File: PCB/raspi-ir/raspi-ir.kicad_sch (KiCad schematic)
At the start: 7 parts, among them J1 Conn_02x16_Odd_Even, J2 Conn_01x02_Pin, Q1 MMBT2222A, U1 TSOP382xx

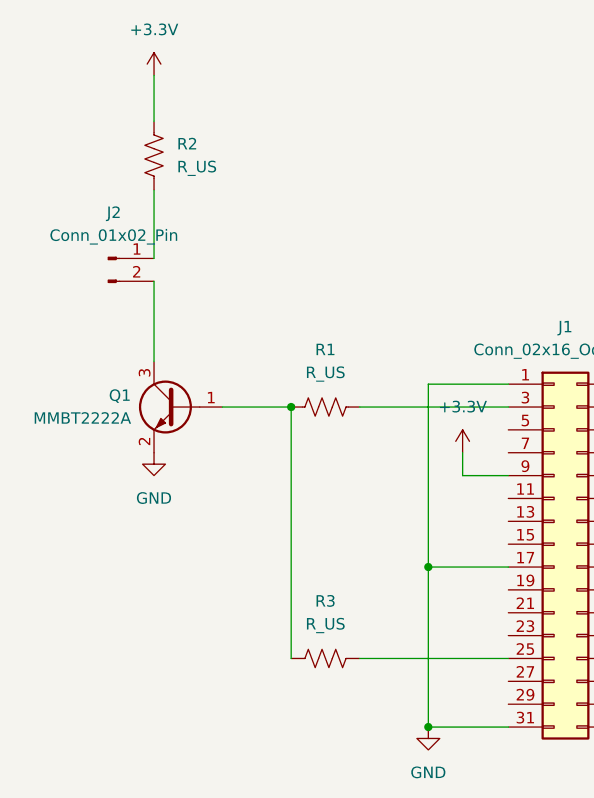
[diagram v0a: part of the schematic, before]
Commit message: New button renderings. Added lirc remotes.
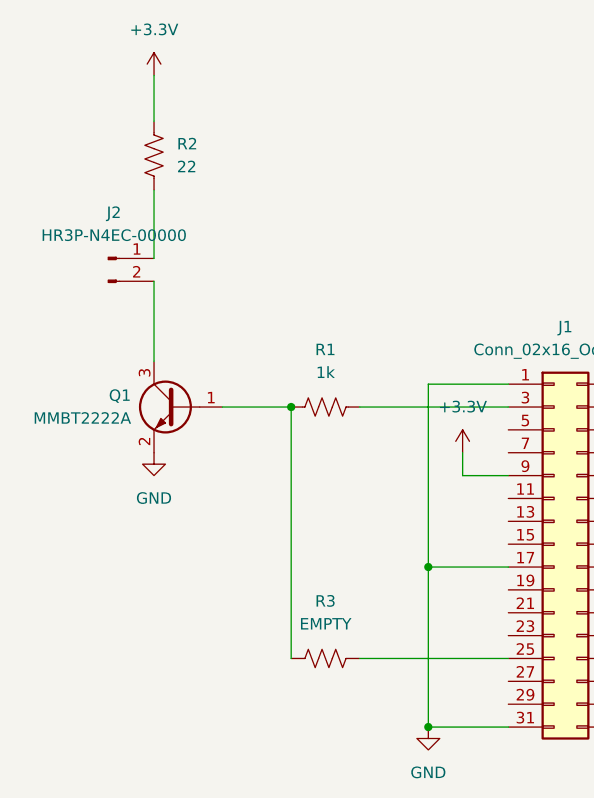
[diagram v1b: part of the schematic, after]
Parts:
- J2: value Conn_01x02_Pin -> HR3P-N4EC-00000; Digikey (none) -> 516-HR3P-N4EC-00000-ND
- R1: value R_US -> 1k
- R2: value R_US -> 22
- R3: value R_US -> EMPTY
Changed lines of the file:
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@@
 			)
 		)
-		(property "Value" "R_US"
+		(property "Value" "EMPTY"
 			(at 120.65 95.25 90)
 			(effects
@@
 			)
 		)
-		(property "Description" "Resistor, US symbol"
+		(property "Description" "Secondary option if PWM output is needed."
 			(at 120.65 99.06 0)
 			(effects
@@
 			)
 		)
-		(property "Value" "R_US"
+		(property "Value" "22"
 			(at 104.14 44.4499 0)
 			(effects
@@
 			)
 		)
-		(property "Value" "R_US"
+		(property "Value" "1k"
 			(at 120.65 67.31 90)
 			(effects
@@
 			)
 		)
-		(property "Value" "Conn_01x02_Pin"
+		(property "Value" "HR3P-N4EC-00000"
 			(at 97.155 52.07 0)
 			(effects
@@
 			)
 		)
-		(property "Description" "Generic connector, single row, 01x02, script generated"
+		(property "Description" "Infrared LED transmitter"
 			(at 96.52 54.61 0)
 			(effects
+				(font
+					(size 1.27 1.27)
+				)
+				(hide yes)
+			)
+		)
+		(property "Digikey" "516-HR3P-N4EC-00000-ND"
+			(at 96.52 54.61 0)
+			(effects

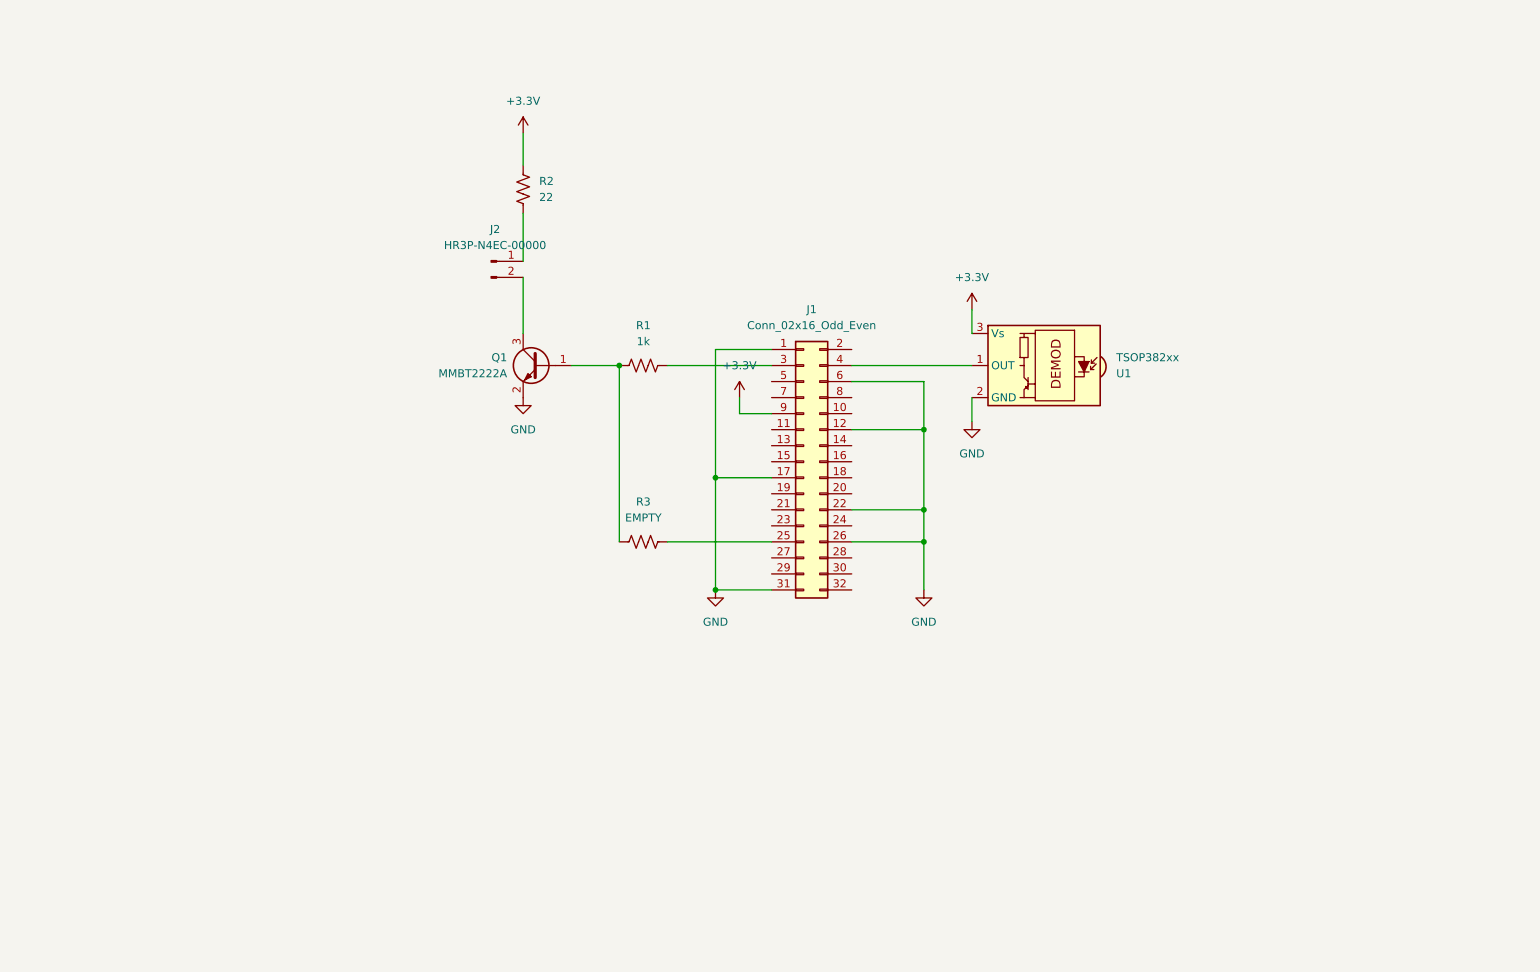
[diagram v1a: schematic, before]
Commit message: Restructured icon files. Updating PCB with more features. Created conference room layout.
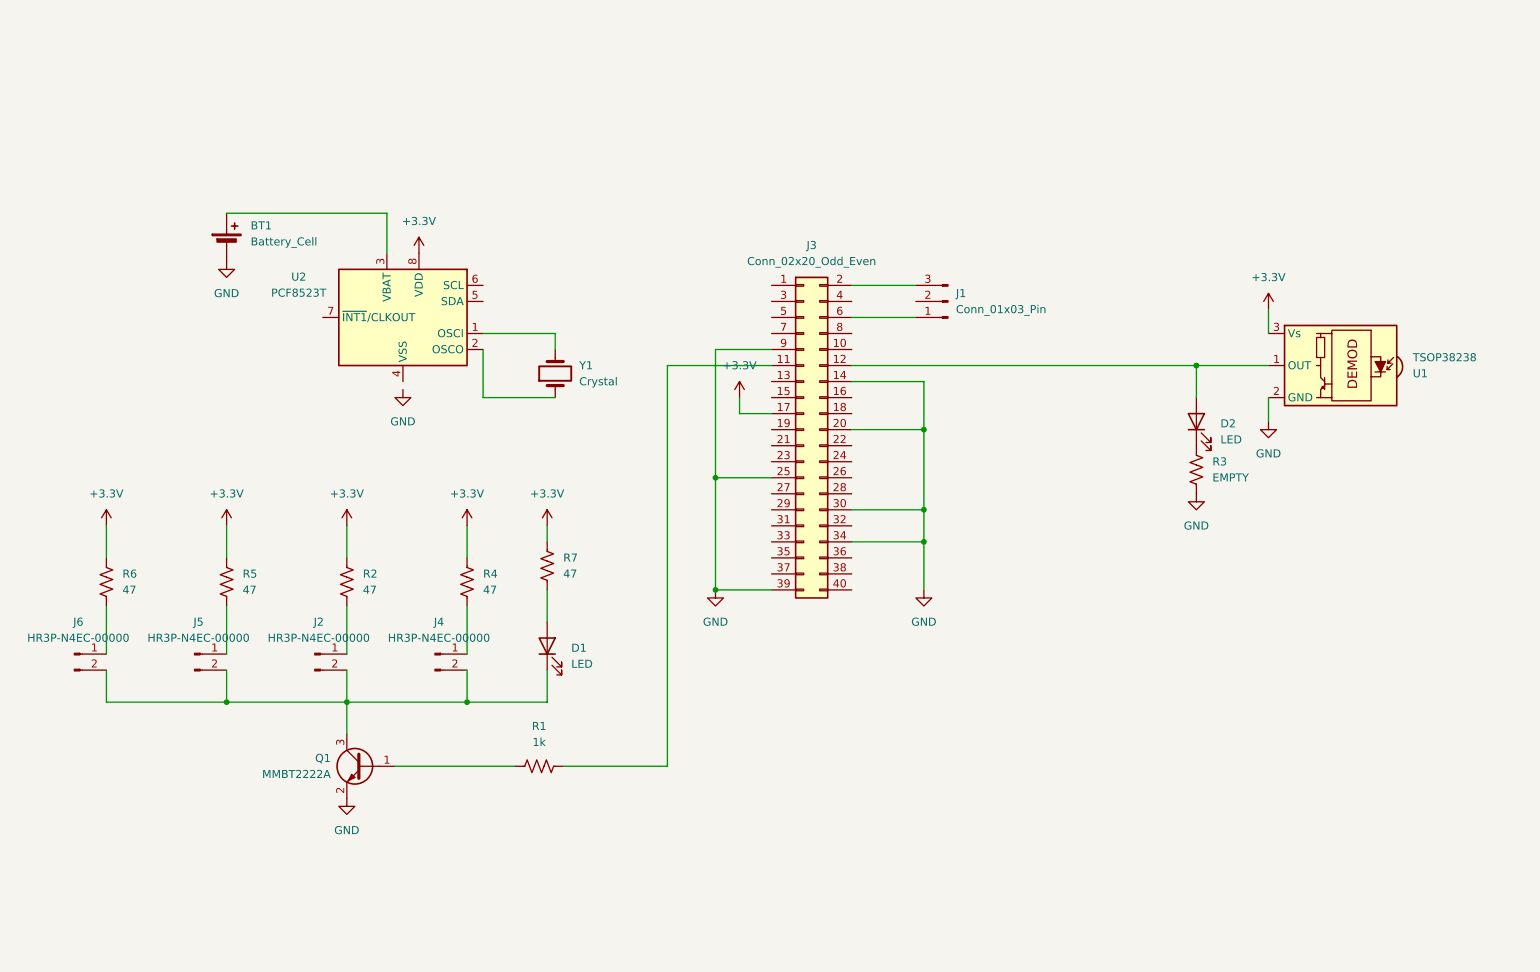
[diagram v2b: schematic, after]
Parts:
- removed J1: Conn_02x16_Odd_Even, Connector_PinHeader_2.54mm:PinHeader_2x16_P2.54mm_Vertical, symbol Connector_Generic:Conn_02x16_Odd_Even
- added BT1: Battery_Cell, Battery:BatteryHolder_Keystone_3000_1x12mm, symbol Device:Battery_Cell
- added D1, D2: LED, Diode_SMD:D_0805_2012Metric, symbol Device:LED
- added J1: Conn_01x03_Pin, Connector_PinSocket_2.54mm:PinSocket_1x03_P2.54mm_Horizontal, symbol Connector:Conn_01x03_Pin
- added J3: Conn_02x20_Odd_Even, Connector_PinHeader_2.54mm:PinHeader_2x20_P2.54mm_Vertical, symbol Connector_Generic:Conn_02x20_Odd_Even
- added J4, J5, J6: HR3P-N4EC-00000, Connector_PinHeader_2.54mm:PinHeader_1x02_P2.54mm_Horizontal, symbol Connector:Conn_01x02_Pin
- added R4, R5, R6, R7: 47, Resistor_SMD:R_0805_2012Metric, symbol Device:R_US
- added U2: PCF8523T, Package_SO:SOIC-8_3.9x4.9mm_P1.27mm, symbol Timer_RTC:PCF8523T
- added Y1: Crystal, Crystal:Crystal_SMD_3215-2Pin_3.2x1.5mm, symbol Device:Crystal
- J2: footprint Connector_PinHeader_2.54mm:PinHeader_1x02_P2.54mm_Vertical -> Connector_PinHeader_2.54mm:PinHeader_1x02_P2.54mm_Horizontal
- Q1: Digikey (none) -> 4878-MMBT2222ATR-ND
- R2: value 22 -> 47; Digikey (none) -> RHM47BTR-ND
- U1: value TSOP382xx -> TSOP38238; Digikey (none) -> 751-1227-ND
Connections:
- net +3.3V: now also J3.17 (Pin_17), R4.1, R5.1, R6.1, R7.1, U2.8 (VDD)
- net GND: now also R3.1, BT1.2 (-), J3.14 (Pin_14), J3.20 (Pin_20), J3.25 (Pin_25), J3.30 (Pin_30), J3.34 (Pin_34), J3.39 (Pin_39), J3.9 (Pin_9)
- net at Q1.1 (B), R1.1: no longer R3.1
- net at R3.2: now also D2.1 (K)
- net at U1.1 (OUT): now also D2.2 (A), J3.12 (Pin_12)
- net at R1.2: now also J3.11 (Pin_11)
- net at J2.2 (Pin_2), Q1.3 (C): now also D1.1 (K), J4.2 (Pin_2), J5.2 (Pin_2), J6.2 (Pin_2)
- new net: J5.1 (Pin_1), R5.2
- new net: BT1.1 (+), U2.3 (VBAT)
- new net: U2.2 (OSCO), Y1.1
- new net: U2.1 (OSCI), Y1.2
- new net: J4.1 (Pin_1), R4.2
- new net: J6.1 (Pin_1), R6.2
- new net: D1.2 (A), R7.2
- new net: J1.1 (Pin_1), J3.6 (Pin_6)
- new net: J1.3 (Pin_3), J3.2 (Pin_2)
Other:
- moved on the sheet: J2, Q1, R1, R2, R3, U1

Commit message: Fix for fan position on case
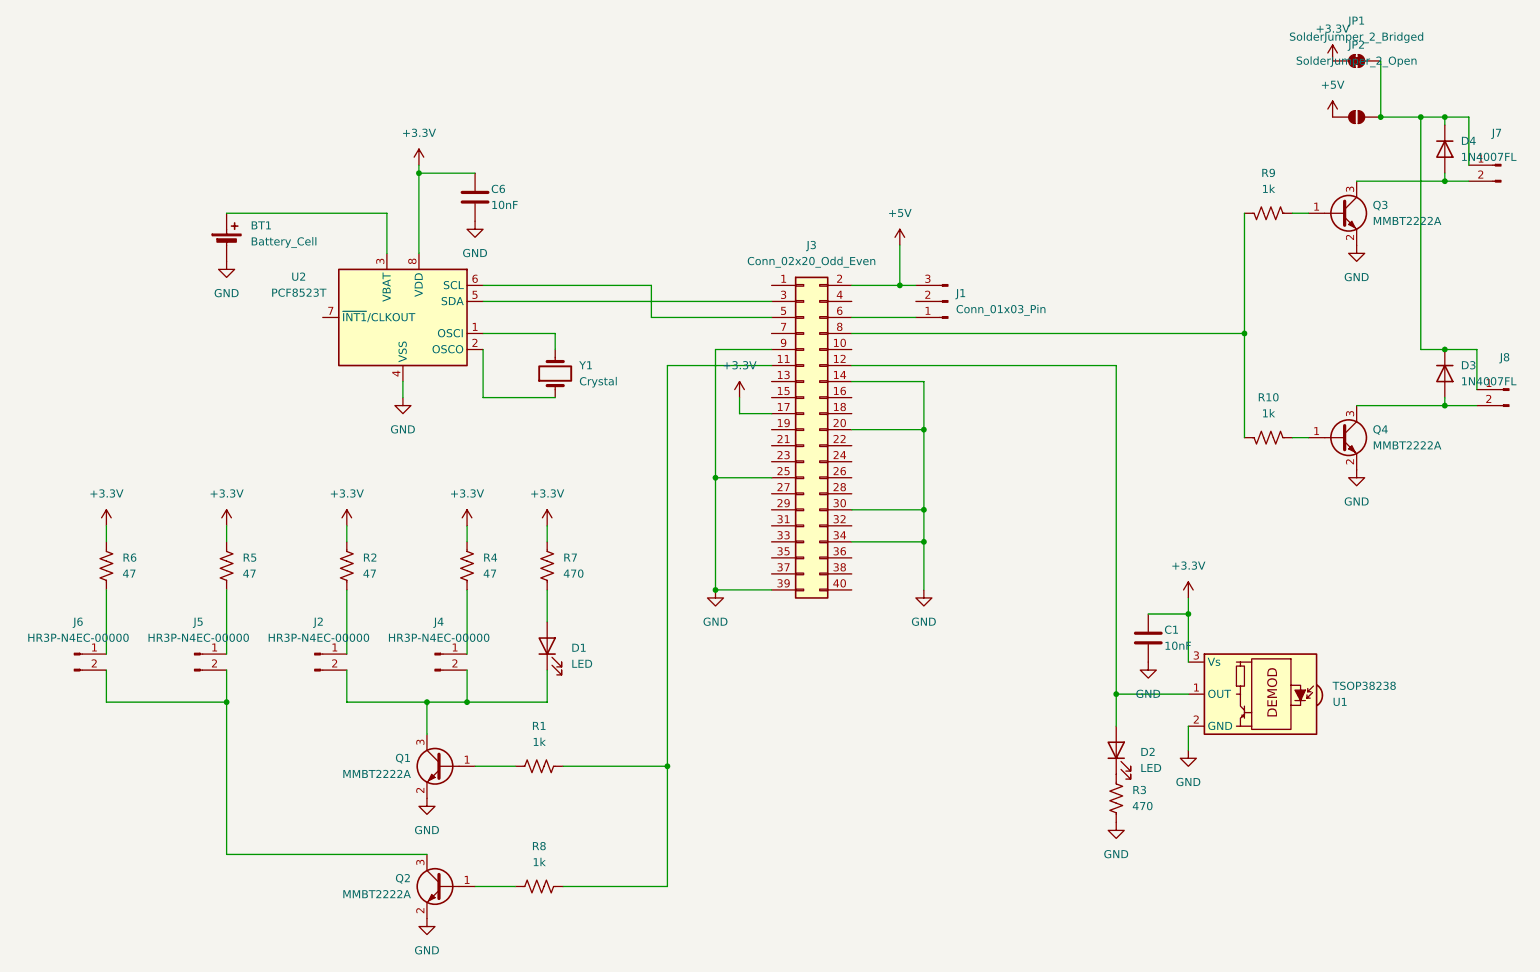
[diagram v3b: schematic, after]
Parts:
- added C1, C6: 10nF, Capacitor_SMD:C_0805_2012Metric, symbol Device:C
- added D3, D4: 1N4007FL, Diode_SMD:D_SOD-123, symbol Diode:MRA4007T3G
- added J7, J8: ~, Connector_PinHeader_2.54mm:PinHeader_1x02_P2.54mm_Horizontal, symbol Connector:Conn_01x02_Pin
- added JP1: SolderJumper_2_Bridged, Jumper:SolderJumper-2_P1.3mm_Bridged2Bar_RoundedPad1.0x1.5mm, symbol Jumper:SolderJumper_2_Bridged
- added JP2: SolderJumper_2_Open, Jumper:SolderJumper-2_P1.3mm_Open_RoundedPad1.0x1.5mm, symbol Jumper:SolderJumper_2_Open
- added Q2, Q3, Q4: MMBT2222A, Package_TO_SOT_SMD:SOT-23, symbol Transistor_BJT:MMBT2222A
- added R10, R8, R9: 1k, Resistor_SMD:R_0805_2012Metric, symbol Device:R_US
- R3: value EMPTY -> 470
- R7: value 47 -> 470; Digikey RHM47BTR-ND -> (none)
- U2: Digikey (none) -> 568-5306-2-ND
- Y1: Digikey (none) -> 535-9543-2-ND
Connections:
- net +3.3V: now also C1.1, C6.1, JP1.1 (A)
- net GND: now also U2.4 (VSS), C1.2, C6.2, Q2.2 (E), Q3.2 (E), Q4.2 (E)
- net at D1.1 (K), J2.2 (Pin_2), J4.2 (Pin_2)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: no longer J5.2 (Pin_2), J6.2 (Pin_2)
- net +5V: now reaches J1.3 (Pin_3), J3.2 (Pin_2)
- net +5V: now also JP2.1 (A)
- net at J3.11 (Pin_11), R1.2: now also R8.2
- net at J3.3 (Pin_3): now also U2.5 (SDA)
- net at J3.5 (Pin_5): now also U2.6 (SCL)
- net at J3.8 (Pin_8): now also R10.2, R9.2
- new net: Q3.1 (B), R9.1
- new net: J5.2 (Pin_2), J6.2 (Pin_2), Q2.3 (C)
- new net: D3.1 (K), D4.1 (K), J7.1 (Pin_1), J8.1 (Pin_1), JP1.2 (B), JP2.2 (B)
- new net: D4.2 (A), J7.2 (Pin_2), Q3.3 (C)
- new net: Q2.1 (B), R8.1
- new net: Q4.1 (B), R10.1
- new net: D3.2 (A), J8.2 (Pin_2), Q4.3 (C)
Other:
- moved on the sheet: D2, Q1, R2, R3, R4, R5, R6, U1

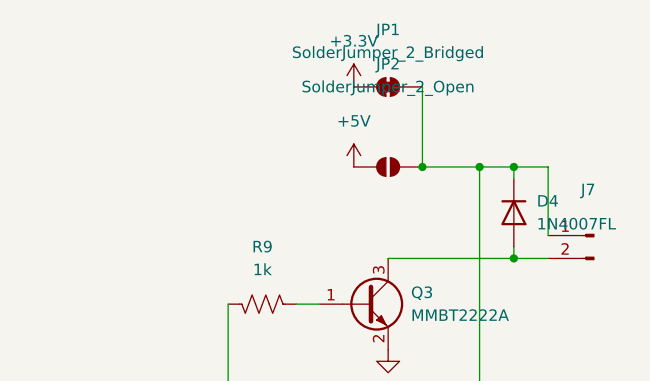
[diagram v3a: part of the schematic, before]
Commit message: Updated conference-room template, created install scripts, finished STL files.
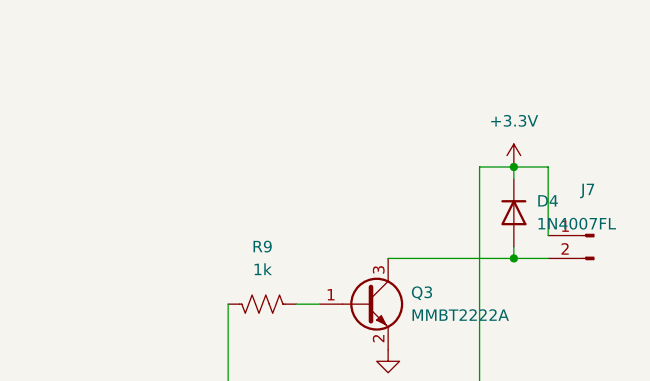
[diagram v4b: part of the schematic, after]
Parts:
- removed JP1: SolderJumper_2_Bridged, Jumper:SolderJumper-2_P1.3mm_Bridged2Bar_RoundedPad1.0x1.5mm, symbol Jumper:SolderJumper_2_Bridged
- removed JP2: SolderJumper_2_Open, Jumper:SolderJumper-2_P1.3mm_Open_RoundedPad1.0x1.5mm, symbol Jumper:SolderJumper_2_Open
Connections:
- net +3.3V: now also D3.1 (K), D4.1 (K), J7.1 (Pin_1), J8.1 (Pin_1)
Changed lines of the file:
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@@
 	)
 	(junction
-		(at 243.84 31.75)
-		(diameter 0)
-		(color 0 0 0 0)
-	)
-	(junction
 		(at 207.01 110.49)
 		(diameter 0)
@@
 		(color 0 0 0 0)
 	)
-	(junction
-		(at 237.49 31.75)
-		(diameter 0)
-		(color 0 0 0 0)
-	)
 	(wire
 		(pts
@@
 	(wire
 		(pts
-			(xy 243.84 31.75) (xy 237.49 31.75)
-		)
-		(stroke
-			(width 0)
-			(type default)
-		)
-	)
-	(wire
-		(pts
 			(xy 35.56 96.52) (xy 35.56 99.06)
 		)
@@
 	(wire
 		(pts
-			(xy 237.49 22.86) (xy 237.49 31.75)
-		)
-		(stroke
-			(width 0)
-			(type default)
-		)
-	)
-	(wire
-		(pts
 			(xy 107.95 153.67) (xy 124.46 153.67)
 		)
@@
 	(symbol
 		(lib_id "power:+3.3V")
-		(at 229.87 22.86 0)
+		(at 247.65 31.75 0)
 		(unit 1)
 		(exclude_from_sim no)
@@
 		(fields_autoplaced yes)
 		(property "Reference" "#PWR021"
-			(at 229.87 26.67 0)
+			(at 247.65 35.56 0)
 			(effects
 				(font
@@
 		)
 		(property "Value" "+3.3V"
-			(at 229.87 17.78 0)
+			(at 247.65 26.67 0)
 			(effects
 				(font
@@
 		)
 		(property "Footprint" ""
-			(at 229.87 22.86 0)
+			(at 247.65 31.75 0)
 			(effects
 				(font
@@
 		)
 		(property "Datasheet" ""
-			(at 229.87 22.86 0)
+			(at 247.65 31.75 0)
 			(effects
 				(font
@@
 		)
 		(property "Description" "Power symbol creates a global label with name \"+3.3V\""
-			(at 229.87 22.86 0)
+			(at 247.65 31.75 0)
 			(effects
 				(font
@@
 	)
 	(symbol
-		(lib_id "power:+5V")
-		(at 229.87 31.75 0)
-		(unit 1)
-		(exclude_from_sim no)
-		(in_bom yes)
-		(on_board yes)
-		(dnp no)
-		(fields_autoplaced yes)
-		(property "Reference" "#PWR020"
-			(at 229.87 35.56 0)
-			(effects
-				(font
-					(size 1.27 1.27)
-				)
-				(hide yes)
-			)
-		)
-		(property "Value" "+5V"
-			(at 229.87 26.67 0)
-			(effects
-				(font
-					(size 1.27 1.27)
-				)
-			)
-		)
-		(property "Footprint" ""
-			(at 229.87 31.75 0)
-			(effects
-				(font
-					(size 1.27 1.27)
-				)
-				(hide yes)
-			)
-		)
-		(property "Datasheet" ""
-			(at 229.87 31.75 0)
-			(effects
-				(font
-					(size 1.27 1.27)
-				)
-				(hide yes)
-			)
-		)
-		(property "Description" "Power symbol creates a global label with name \"+5V\""
-			(at 229.87 31.75 0)
-			(effects
-				(font
-					(size 1.27 1.27)
-				)
-				(hide yes)
-			)
-		)
-		(pin "1"
-		)
-		(instances
-			(project "raspi-ir"
-				(path "/44299703-577c-4e07-82b2-1ac696b0eb61"
-					(reference "#PWR020")
-					(unit 1)
-				)
-			)
-		)
-	)
-	(symbol
 		(lib_id "power:GND")
 		(at 195.58 143.51 0)
@@
 	)
 	(symbol
-		(lib_id "Jumper:SolderJumper_2_Bridged")
-		(at 233.68 22.86 0)
-		(unit 1)
-		(exclude_from_sim no)
-		(in_bom no)
-		(on_board yes)
-		(dnp no)
-		(fields_autoplaced yes)
-		(property "Reference" "JP1"
-			(at 233.68 16.51 0)
-			(effects
-				(font
-					(size 1.27 1.27)
-				)
-			)
-		)
-		(property "Value" "SolderJumper_2_Bridged"
-			(at 233.68 19.05 0)
-			(effects
-				(font
-					(size 1.27 1.27)
-				)
-			)
-		)
-		(property "Footprint" "Jumper:SolderJumper-2_P1.3mm_Bridged2Bar_RoundedPad1.0x1.5mm"
-			(at 233.68 22.86 0)
-			(effects
-				(font
-					(size 1.27 1.27)
-				)
-				(hide yes)
-			)
-		)
-		(property "Datasheet" "~"
-			(at 233.68 22.86 0)
-			(effects
-				(font
-					(size 1.27 1.27)
-				)
-				(hide yes)
-			)
-		)
-		(property "Description" "Solder Jumper, 2-pole, closed/bridged"
-			(at 233.68 22.86 0)
-			(effects
-				(font
-					(size 1.27 1.27)
-				)
-				(hide yes)
-			)
-		)
-		(pin "2"
-		)
-		(pin "1"
-		)
-		(instances
-			(project ""
-				(path "/44299703-577c-4e07-82b2-1ac696b0eb61"
-					(reference "JP1")
-					(unit 1)
-				)
-			)
-		)
-	)
-	(symbol
 		(lib_id "power:+3.3V")
 		(at 73.66 96.52 0)
@@
 					(unit 1)
 				)
-			)
-		)
-	)
-	(symbol
-		(lib_id "Jumper:SolderJumper_2_Open")
-		(at 233.68 31.75 0)
-		(unit 1)
-		(exclude_from_sim no)
-		(in_bom no)
-		(on_board yes)
-		(dnp no)
-		(property "Reference" "JP2"
-			(at 233.68 20.32 0)
-			(effects
-				(font
-					(size 1.27 1.27)
-				)
-			)
-		)
-		(property "Value" "SolderJumper_2_Open"
-			(at 233.68 22.86 0)
-			(effects
-				(font
-					(size 1.27 1.27)
-				)
-			)
-		)
-		(property "Footprint" "Jumper:SolderJumper-2_P1.3mm_Open_RoundedPad1.0x1.5mm"
-			(at 233.68 31.75 0)
-			(effects
-				(font
-					(size 1.27 1.27)
-				)
-				(hide yes)
-			)
-		)
-		(property "Datasheet" "~"
-			(at 233.68 31.75 0)
-			(effects
-				(font
-					(size 1.27 1.27)
-				)
-				(hide yes)
-			)
-		)
-		(property "Description" "Solder Jumper, 2-pole, open"
-			(at 233.68 31.75 0)
-			(effects
-				(font
-					(size 1.27 1.27)
-				)
-				(hide yes)
-			)
-		)
-		(pin "2"
-		)
-		(pin "1"
-		)
-		(instances
-			(project ""
-				(path "/44299703-577c-4e07-82b2-1ac696b0eb61"
-					(reference "JP2")
-					(unit 1)
-				)
